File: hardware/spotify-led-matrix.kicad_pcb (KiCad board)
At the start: 2 copper layers, 192 x 264 mm, 81 parts, among them J1 +5V, J2 DISPLAY_IN, J4 DISPLAY_OUT, J5 USB_C_Receptacle_USB2.0, Q1 IRLML6244TRPBF, Q2 SS8050-G, Q3 SS8050-G, Q4 IRLML6244TRPBF, Q5 IRLML6244TRPBF, Q6 IRLML6244TRPBF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

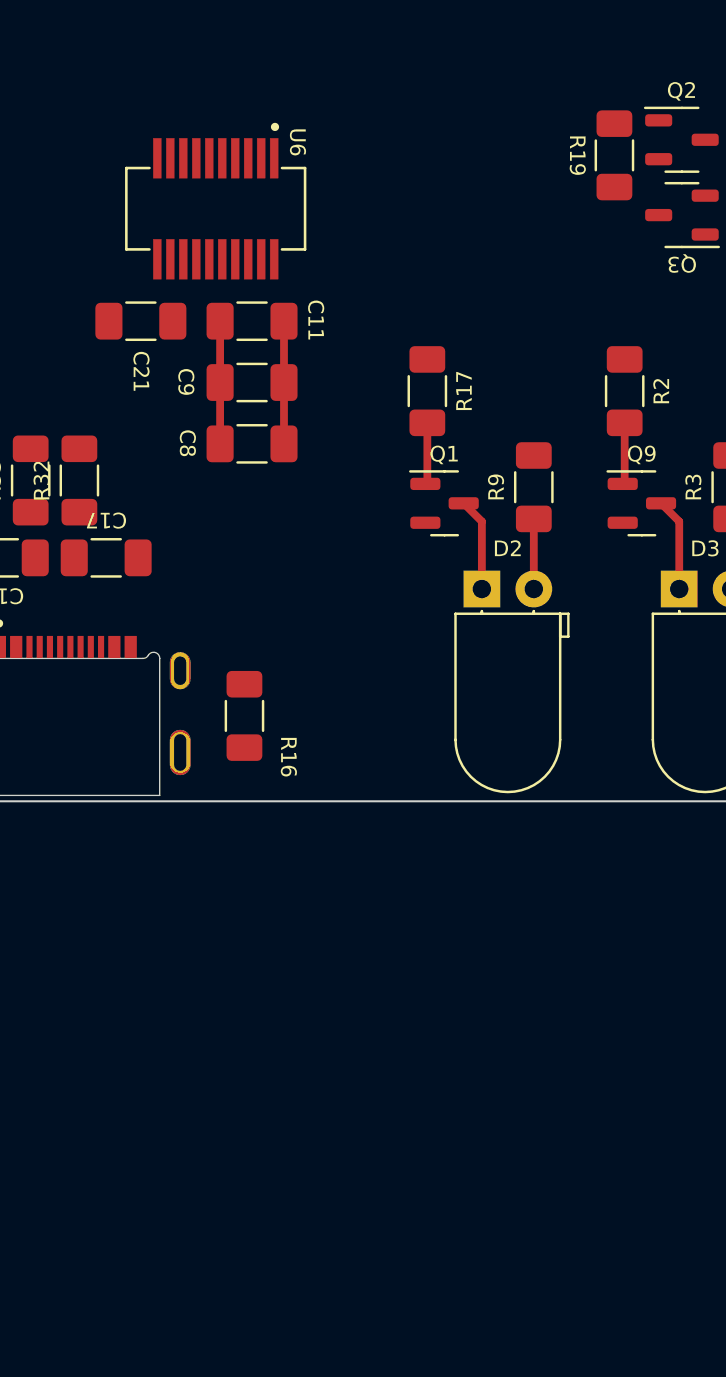
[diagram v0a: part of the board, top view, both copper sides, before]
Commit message: reformatted schematic and changed parts: - added new voltage regulator: 1117 adjustable (jellybean) - added temp/volt/cur sensor LTC2990 - changed usb to uart IC to SSOP20 footprint - created and added the display connector symbols
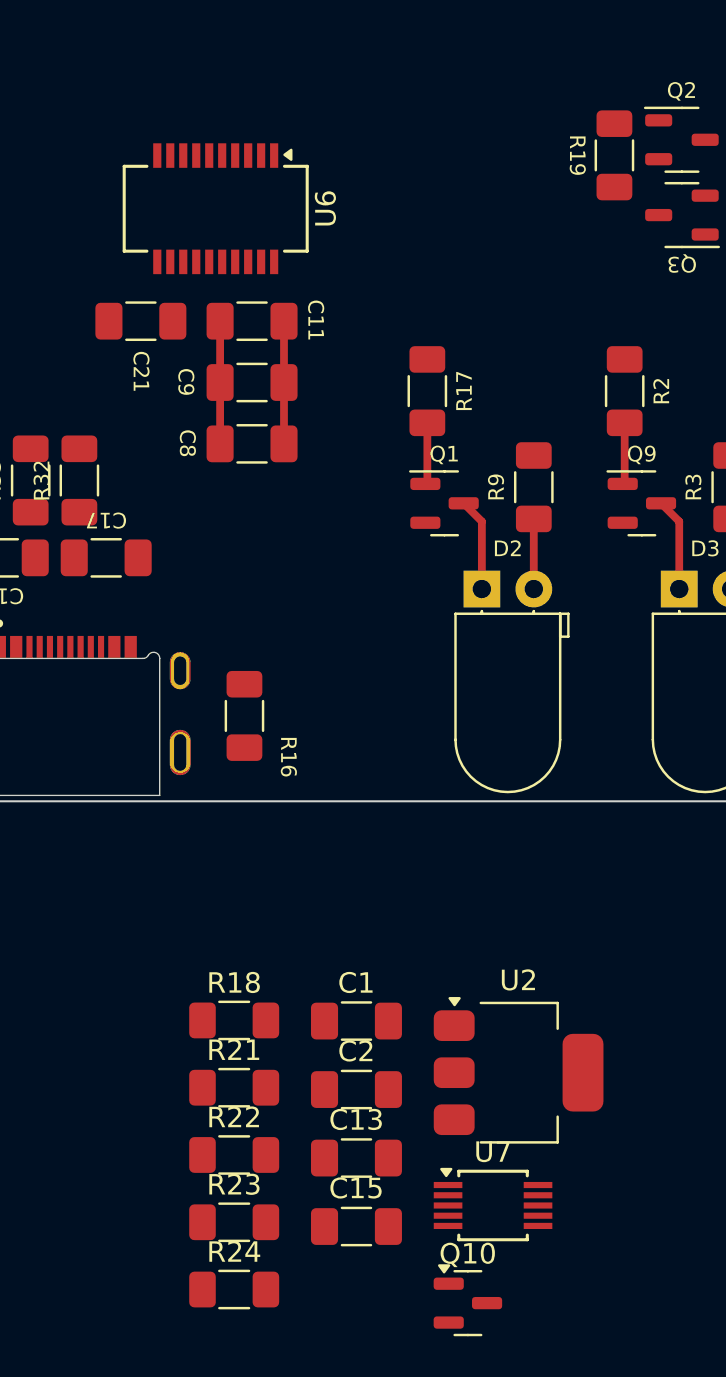
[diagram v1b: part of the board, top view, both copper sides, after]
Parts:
- added C1: 10uF, Capacitor_SMD:C_1206_3216Metric_Pad1.33x1.80mm_HandSolder, F.Cu at (169.4, 330.2)
- added C13: 470pF, Capacitor_SMD:C_1206_3216Metric_Pad1.33x1.80mm_HandSolder, F.Cu at (169.4, 336.9)
- added C15: 0.1uF, Capacitor_SMD:C_1206_3216Metric_Pad1.33x1.80mm_HandSolder, F.Cu at (169.4, 340.3)
- added C2: 10uF, Capacitor_SMD:C_1206_3216Metric_Pad1.33x1.80mm_HandSolder, F.Cu at (169.4, 333.6)
- added Q10: MMBT3904, Package_TO_SOT_SMD:SOT-23, F.Cu at (174.8, 344.0)
- added R18: ~, Resistor_SMD:R_1206_3216Metric_Pad1.30x1.75mm_HandSolder, F.Cu at (163.4, 330.2)
- added R21: ~, Resistor_SMD:R_1206_3216Metric_Pad1.30x1.75mm_HandSolder, F.Cu at (163.4, 333.5)
- added R22: 1m, Resistor_SMD:R_1206_3216Metric_Pad1.30x1.75mm_HandSolder, F.Cu at (163.4, 336.8)
- added R23: 4.7k, Resistor_SMD:R_1206_3216Metric_Pad1.30x1.75mm_HandSolder, F.Cu at (163.4, 340.1)
- added R24: 4.7k, Resistor_SMD:R_1206_3216Metric_Pad1.30x1.75mm_HandSolder, F.Cu at (163.4, 343.4)
- added U2: NCP1117-ADJ, Package_TO_SOT_SMD:SOT-223-3_TabPin2, F.Cu at (177.3, 332.8)
- added U7: LTC2990, Package_SO:MSOP-10_3x3mm_P0.5mm, F.Cu at (176.1, 339.3)
- U6: footprint spotify-led-matrix:SOP63P599X175-20N -> Package_SO:SSOP-20_3.9x8.7mm_P0.635mm
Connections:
- net /CLK renamed /SPI_CLK
- U1 pad 10: /ROTARY_B -> /MODE_SELECT
- U1 pad 11: /ROTARY_A -> /ROTARY_B
- U1 pad 12: unconnected-(U1-IO27-Pad12) -> /ROTARY_A
- U1 pad 8: unconnected-(U1-IO32-Pad8) -> /OSC_IN
- U1 pad 9: /MODE_SELECT -> /OSC_OUT

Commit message: lots of changes: working on finalizing everything!
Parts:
- removed the C1 at (169.4, 330.2)
- removed the C1 at (222.4, 292.3)
- removed C13: 470pF, Capacitor_SMD:C_1206_3216Metric_Pad1.33x1.80mm_HandSolder
- removed C15: 0.1uF, Capacitor_SMD:C_1206_3216Metric_Pad1.33x1.80mm_HandSolder
- removed the C2 at (169.4, 333.6)
- removed the C2 at (210.2, 292.3)
- removed F1: 6A, Fuse:Fuse_1206_3216Metric_Pad1.42x1.75mm_HandSolder
- removed Q10: MMBT3904, Package_TO_SOT_SMD:SOT-23
- removed R22: 1m, Resistor_SMD:R_1206_3216Metric_Pad1.30x1.75mm_HandSolder
- removed R23, R24: 4.7k, Resistor_SMD:R_1206_3216Metric_Pad1.30x1.75mm_HandSolder
- removed TP6: +3V3, TestPoint:TestPoint_Loop_D2.54mm_Drill1.5mm_Beaded
- removed the U2 at (177.3, 332.8)
- removed the U2 at (216.3, 292.3)
- removed U7: LTC2990, Package_SO:MSOP-10_3x3mm_P0.5mm
- added C1: 10uF, Capacitor_SMD:C_1206_3216Metric_Pad1.33x1.80mm_HandSolder, F.Cu at (227.1, 295.0)
- added C2: 10uF, Capacitor_SMD:C_1206_3216Metric_Pad1.33x1.80mm_HandSolder, F.Cu at (220.3, 299.2)
- added REF**: Mounting_Wuerth_WA-SMSI-M3_H12mm_9774120360, Mounting_Wuerth:Mounting_Wuerth_WA-SMSI-M3_H12mm_9774120360, F.Cu at (108.6, 262.5)
- added REF**: Mounting_Wuerth_WA-SMSI-M3_H12mm_9774120360, Mounting_Wuerth:Mounting_Wuerth_WA-SMSI-M3_H12mm_9774120360, F.Cu at (216.3, 309.5)
- added REF**: Mounting_Wuerth_WA-SMSI-M3_H12mm_9774120360, Mounting_Wuerth:Mounting_Wuerth_WA-SMSI-M3_H12mm_9774120360, F.Cu at (218.9, 266.2)
- added REF**: Mounting_Wuerth_WA-SMSI-M3_H12mm_9774120360, Mounting_Wuerth:Mounting_Wuerth_WA-SMSI-M3_H12mm_9774120360, F.Cu at (102.3, 312.1)
- added TP1: +5V, TestPoint:TestPoint_Pad_D2.0mm, F.Cu at (233.3, 297.6)
- added TP2: GND, TestPoint:TestPoint_Pad_D2.0mm, F.Cu at (233.3, 292.1)
- added TP3: +3V3, TestPoint:TestPoint_Pad_D2.0mm, F.Cu at (210.8, 291.1)
- added U2: NCP1117-ADJ, Package_TO_SOT_SMD:SOT-223-3_TabPin2, F.Cu at (221.9, 293.4)
- Q2, Q3: footprint Package_TO_SOT_SMD:SOT-23-3 -> Package_TO_SOT_SMD:SOT-23
- TP4: value +5V -> BOOT; footprint TestPoint:TestPoint_Loop_D2.54mm_Drill1.5mm_Beaded -> TestPoint:TestPoint_Pad_D2.0mm
- TP5: value GND -> EN; footprint TestPoint:TestPoint_Loop_D2.54mm_Drill1.5mm_Beaded -> TestPoint:TestPoint_Pad_D2.0mm
- moved R18 65.1 mm to (216.8, 292.9), turned to 90 degrees
- moved R21 63.8 mm to (215.5, 296.6)
- moved TP5 56.1 mm to (184.0, 274.1)
- moved TP4 24.9 mm to (211.5, 283.8)
- moved R12 12.8 mm to (182.4, 262.9), turned to 90 degrees
- moved R10 8.07 mm to (182.4, 268.5)
- moved C19 6.05 mm to (158.1, 308.3), turned to 0 degrees
- moved C17 4.67 mm to (152.5, 308.3), turned to 180 degrees
- moved C21 3.56 mm to (160.4, 299.2), turned to -90 degrees
- moved R33 3.13 mm to (156.5, 304.5)
- moved R32 1.91 mm to (154.1, 304.5)
- moved J5 0.50 mm to (155.4, 317.5)
- moved R16 0.24 mm to (163.9, 315.1)
- moved R25 0.14 mm to (114.0, 289.4)
- moved C12 0.14 mm to (123.8, 292.5)
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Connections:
- net /B1_OUT renamed /B2_IN
- net /G1_OUT renamed /G2_IN
- net /MODE_SELECT renamed /BUTTON
- net /R1_IN renamed /SPI_SDA
- net /R1_OUT renamed /R2_IN
- J2 pad 16: /LAT -> /~{LAT}
- TP4 pad 1: +5V -> /BOOT
- TP5 pad 1: GND -> /EN
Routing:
- net Net-(D7-A): track 6.80 -> 82.8 mm
- net /ROTARY_A: track 3.38 -> 78.0 mm
- net /ROTARY_B: track 3.38 -> 70.5 mm
- net Net-(D6-A): track 6.94 -> 68.5 mm
- net /BUTTON: track 3.35 -> 62.9 mm
- net /DEV: track 0.00 -> 44.3 mm
- net /VOLUME: track 0.00 -> 40.0 mm
- net Net-(D5-A): track 6.80 -> 44.3 mm
- net /RXD0: track 0.00 -> 34.4 mm
- net /TXD0: track 0.00 -> 32.5 mm
- net /RTS: track 0.00 -> 26.1 mm
- net /DTR: track 0.00 -> 20.9 mm
- net +3V3: track 19.4 -> 0.00 mm
- net GND: track 9.60 -> 23.1 mm, vias 0 -> 13
- net /EN: track 7.49 -> 0.00 mm
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- added copper zone on F.Cu, net +3V3
- added copper zone on F.Cu, net +5V
- added copper zone on F.Cu, net GND
- added copper zone on F.Cu, net Net-(U2-ADJ)

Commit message: update?
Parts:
- added R22: 22, Resistor_SMD:R_1206_3216Metric_Pad1.30x1.75mm_HandSolder, F.Cu at (188.5, 279.5)
- added R23: 22, Resistor_SMD:R_1206_3216Metric_Pad1.30x1.75mm_HandSolder, F.Cu at (195.7, 283.8)
- moved TP5 9.80 mm to (178.9, 265.7)
- moved REF** 3.28 mm to (216.2, 312.8)
- moved R14 2.94 mm to (214.8, 278.6)
- moved R8 2.81 mm to (214.8, 281.1)
- moved C21 2.42 mm to (160.2, 296.8)
- moved C8 1.80 mm to (164.1, 300.2)
- moved C9 1.22 mm to (164.1, 297.8)
- moved C11 0.65 mm to (164.1, 295.4)
- moved R19 0.13 mm to (182.0, 288.0)
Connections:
- R10 pad 2: /EN_AUTO -> /EN_SW
- R12 pad 2: /EN_SW -> /EN_AUTO
- R14 pad 2: /BOOT_AUTO -> /BOOT_SW
- R8 pad 2: /BOOT_SW -> /BOOT_AUTO
- U1 pad 13: /SPI_CLK -> Net-(U1-IO14)
- U1 pad 16: /SPI_SDA -> Net-(U1-IO13)
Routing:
- net GND: track 23.1 -> 12.4 mm, vias 13 -> 9
- net Net-(D6-A): track 68.5 -> 71.3 mm
- net Net-(D7-A): track 82.8 -> 84.7 mm
- net /DTR: track 20.9 -> 22.4 mm
- net Net-(D5-A): track 44.3 -> 45.6 mm
- net /RTS: track 26.1 -> 27.2 mm
- added copper zone on B.Cu, net GND
